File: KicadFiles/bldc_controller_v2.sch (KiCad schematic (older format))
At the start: 172 parts, among them J1 Conn_01x05_Male, J10 Conn_01x02_Female, J11 Conn_01x02_Female, J12 Conn_01x02_Female, J13 Conn_01x02_Female, J14 Conn_01x02_Female, J15 Conn_01x04_Male, J2 Conn_01x03_Male, J3 Conn_01x03_Male, J4 1935174, J5 Conn_01x02_Female, J9 Conn_01x02_Female, Q10 IRLB8721PBF, Q11 IRLB8721PBF, Q2 DMN65D8L-7, Q3 DMN65D8L-7, Q5 IRF4905, Q6 IRLB8721PBF, Q7 IRLB8721PBF, Q8 IRLB8721PBF, Q9 IRLB8721PBF, SW2 D6C40 F1 LFS, SW3 1301.9314, SW4 1301.9314, SW5 SW_Push_DPDT, U1 ATmega328P-PU, U2 uA7810, U3 LM7805_TO220, U4 MCP601-xP, U5 LM339, U6 IRS2004, U7 IRS2004, U8 IRS2004, U9 HCPL-181-00DE, Y1 9B-16.000MBBK-B

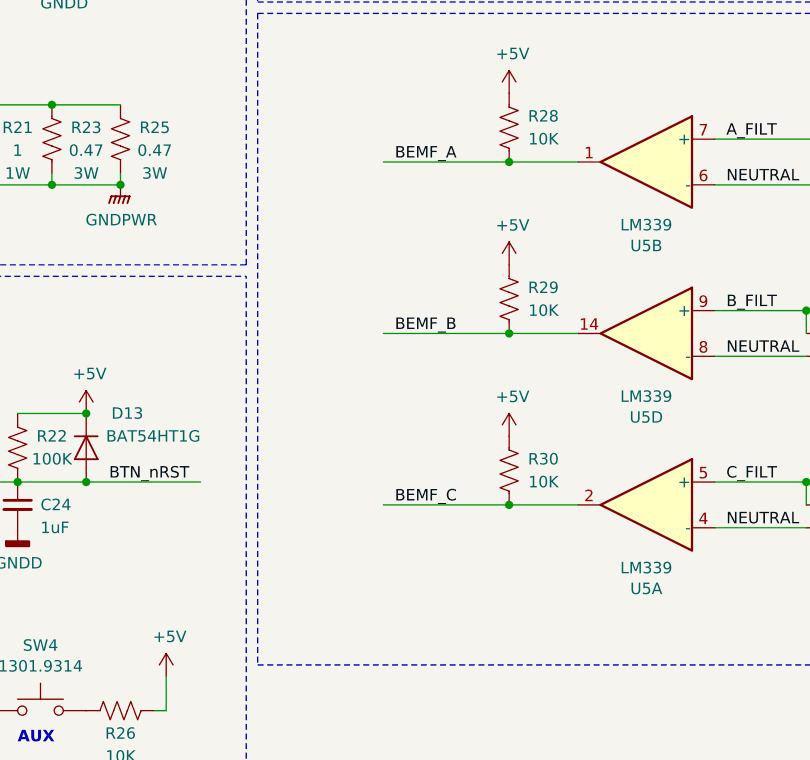
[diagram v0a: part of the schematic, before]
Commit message: Added Caps to BEMF Lines
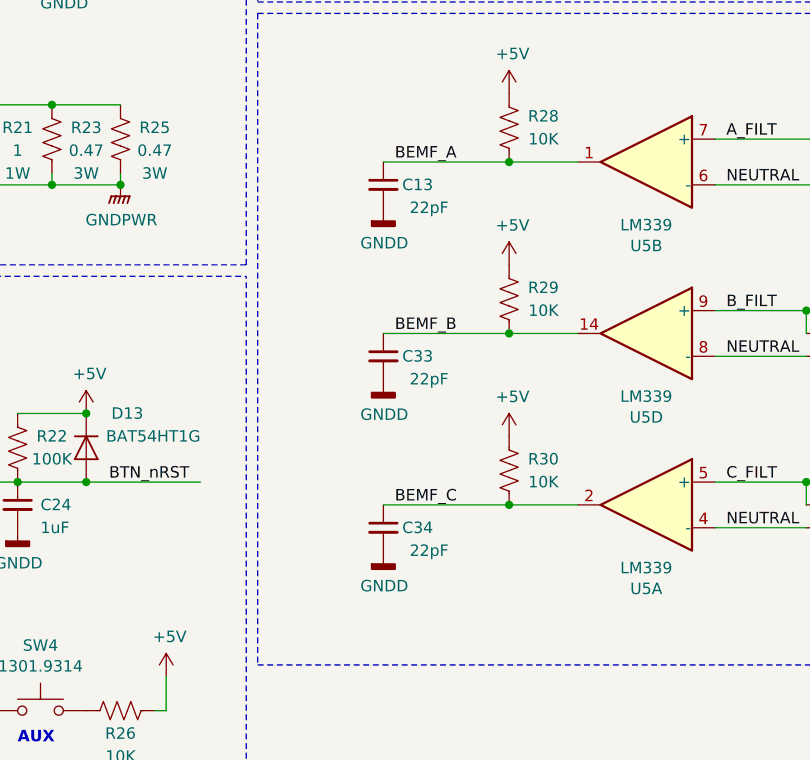
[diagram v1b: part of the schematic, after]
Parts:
- added C13, C33, C34: 22pF, Capacitor_SMD:C_0805_2012Metric_Pad1.15x1.40mm_HandSolder, symbol Device:C_Small
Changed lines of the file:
@@
 Wire Wire Line
 	8400 5850 8850 5850
+$Comp
+L Device:C_Small C33
+U 1 1 5E113FE6
+P 10500 7850
+F 0 "C33" H 10650 7850 50  0000 C CNN
+F 1 "22pF" H 10700 7750 50  0000 C CNN
+F 2 "Capacitor_SMD:C_0805_2012Metric_Pad1.15x1.40mm_HandSolder" H 10500 7850 50  0001 C CNN
+F 3 "~" H 10500 7850 50  0001 C CNN
+	1    10500 7850
+	1    0    0    -1
+$EndComp
+$Comp
+L power:GNDD #PWR026
+U 1 1 5E118132
+P 10500 7950
+F 0 "#PWR026" H 10500 7700 50  0001 C CNN
+F 1 "GNDD" H 10504 7795 50  0000 C CNN
+F 2 "" H 10500 7950 50  0001 C CNN
+F 3 "" H 10500 7950 50  0001 C CNN
+	1    10500 7950
+	1    0    0    -1
+$EndComp
+$Comp
+L Device:C_Small C34
+U 1 1 5E11899C
+P 10500 8600
+F 0 "C34" H 10650 8600 50  0000 C CNN
+F 1 "22pF" H 10700 8500 50  0000 C CNN
+F 2 "Capacitor_SMD:C_0805_2012Metric_Pad1.15x1.40mm_HandSolder" H 10500 8600 50  0001 C CNN
+F 3 "~" H 10500 8600 50  0001 C CNN
+	1    10500 8600
+	1    0    0    -1
+$EndComp
+$Comp
+L power:GNDD #PWR054
+U 1 1 5E1189A6
+P 10500 8700
+F 0 "#PWR054" H 10500 8450 50  0001 C CNN
+F 1 "GNDD" H 10504 8545 50  0000 C CNN
+F 2 "" H 10500 8700 50  0001 C CNN
+F 3 "" H 10500 8700 50  0001 C CNN
+	1    10500 8700
+	1    0    0    -1
+$EndComp
+$Comp
+L Device:C_Small C13
+U 1 1 5E13EF98
+P 10500 7100
+F 0 "C13" H 10650 7100 50  0000 C CNN
+F 1 "22pF" H 10700 7000 50  0000 C CNN
+F 2 "Capacitor_SMD:C_0805_2012Metric_Pad1.15x1.40mm_HandSolder" H 10500 7100 50  0001 C CNN
+F 3 "~" H 10500 7100 50  0001 C CNN
+	1    10500 7100
+	1    0    0    -1
+$EndComp
+$Comp
+L power:GNDD #PWR025
+U 1 1 5E13EFA2
+P 10500 7200
+F 0 "#PWR025" H 10500 6950 50  0001 C CNN
+F 1 "GNDD" H 10504 7045 50  0000 C CNN
+F 2 "" H 10500 7200 50  0001 C CNN
+F 3 "" H 10500 7200 50  0001 C CNN
+	1    10500 7200
+	1    0    0    -1
+$EndComp
 $EndSCHEMATC

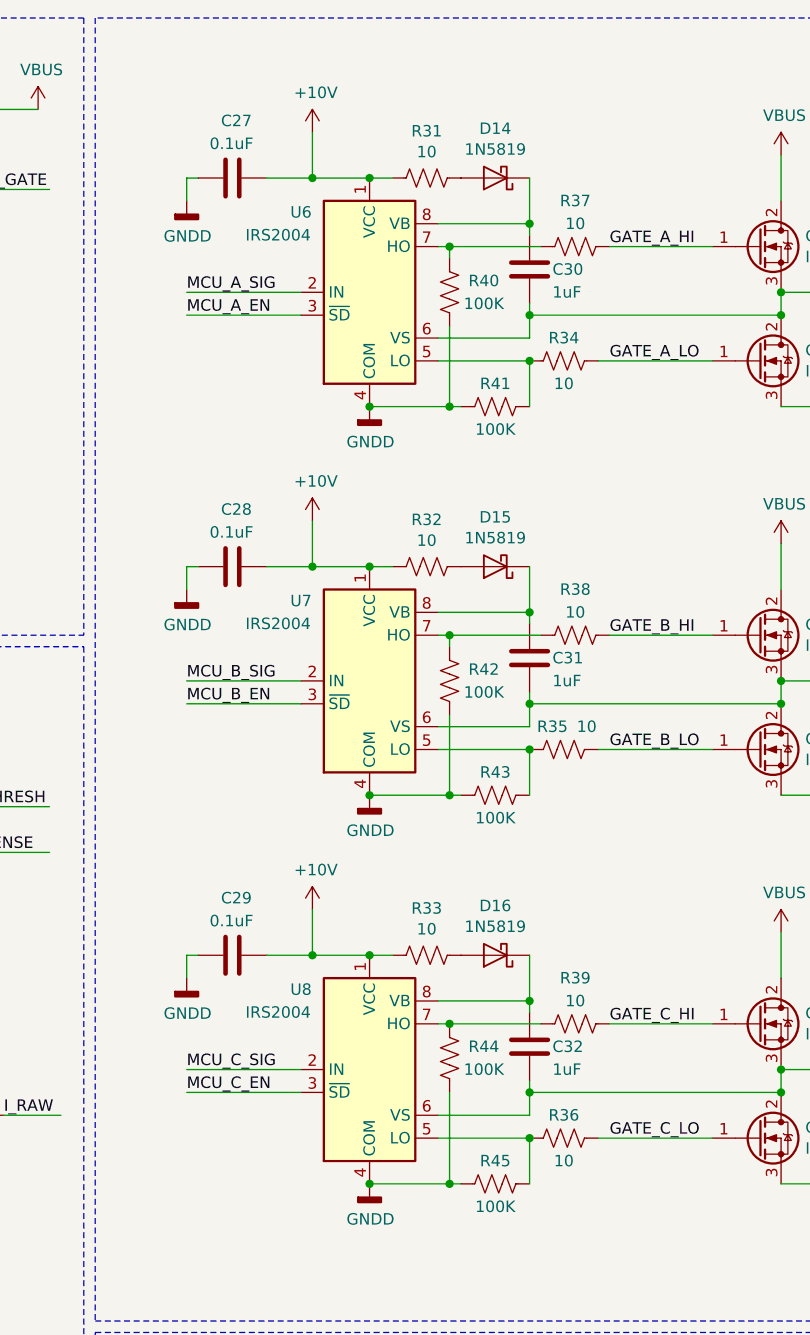
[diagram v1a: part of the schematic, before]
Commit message: Fixed Charge Pumps and Added Text
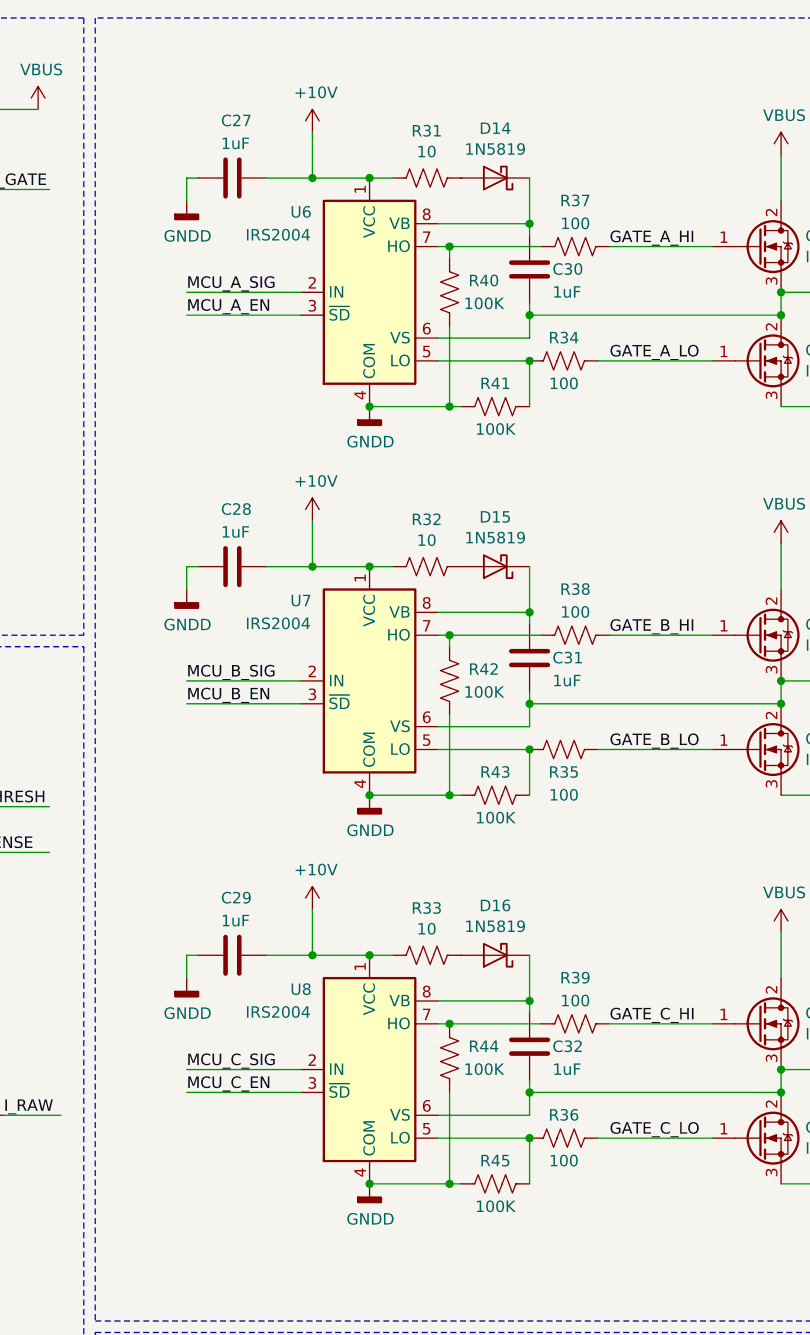
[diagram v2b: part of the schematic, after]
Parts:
- C27, C28, C29: value 0.1uF -> 1uF
- R34, R35, R36, R37, R38, R39: value 10 -> 100
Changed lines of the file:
@@
 P 10550 1300
 F 0 "C27" V 10300 1350 50  0000 R CNN
-F 1 "0.1uF" V 10400 1400 50  0000 R CNN
+F 1 "1uF" V 10400 1350 50  0000 R CNN
 F 2 "Capacitor_SMD:C_0805_2012Metric_Pad1.15x1.40mm_HandSolder" H 10588 1150 50  0001 C CNN
 F 3 "~" H 10550 1300 50  0001 C CNN
@@
 P 12050 1600
 F 0 "R37" V 11850 1600 50  0000 C CNN
-F 1 "10" V 11950 1600 50  0000 C CNN
+F 1 "100" V 11950 1600 50  0000 C CNN
 F 2 "Resistor_SMD:R_0805_2012Metric_Pad1.15x1.40mm_HandSolder" V 12090 1590 50  0001 C CNN
 F 3 "~" H 12050 1600 50  0001 C CNN
@@
 P 12000 2100
 F 0 "R34" V 11900 2100 50  0000 C CNN
-F 1 "10" V 12100 2100 50  0000 C CNN
+F 1 "100" V 12100 2100 50  0000 C CNN
 F 2 "Resistor_SMD:R_0805_2012Metric_Pad1.15x1.40mm_HandSolder" V 12040 2090 50  0001 C CNN
 F 3 "~" H 12000 2100 50  0001 C CNN
@@
 P 10550 3000
 F 0 "C28" V 10300 3050 50  0000 R CNN
-F 1 "0.1uF" V 10400 3100 50  0000 R CNN
+F 1 "1uF" V 10400 3050 50  0000 R CNN
 F 2 "Capacitor_SMD:C_0805_2012Metric_Pad1.15x1.40mm_HandSolder" H 10588 2850 50  0001 C CNN
 F 3 "~" H 10550 3000 50  0001 C CNN
@@
 P 12050 3300
 F 0 "R38" V 11850 3300 50  0000 C CNN
-F 1 "10" V 11950 3300 50  0000 C CNN
+F 1 "100" V 11950 3300 50  0000 C CNN
 F 2 "Resistor_SMD:R_0805_2012Metric_Pad1.15x1.40mm_HandSolder" V 12090 3290 50  0001 C CNN
 F 3 "~" H 12050 3300 50  0001 C CNN
@@
 U 1 1 6071FE0F
 P 12000 3800
-F 0 "R35" V 11900 3750 50  0000 C CNN
-F 1 "10" V 11900 3900 50  0000 C CNN
+F 0 "R35" V 12100 3800 50  0000 C CNN
+F 1 "100" V 12200 3800 50  0000 C CNN
 F 2 "Resistor_SMD:R_0805_2012Metric_Pad1.15x1.40mm_HandSolder" V 12040 3790 50  0001 C CNN
 F 3 "~" H 12000 3800 50  0001 C CNN
@@
 P 10550 4700
 F 0 "C29" V 10300 4750 50  0000 R CNN
-F 1 "0.1uF" V 10400 4800 50  0000 R CNN
+F 1 "1uF" V 10400 4750 50  0000 R CNN
 F 2 "Capacitor_SMD:C_0805_2012Metric_Pad1.15x1.40mm_HandSolder" H 10588 4550 50  0001 C CNN
 F 3 "~" H 10550 4700 50  0001 C CNN
@@
 P 12050 5000
 F 0 "R39" V 11850 5000 50  0000 C CNN
-F 1 "10" V 11950 5000 50  0000 C CNN
+F 1 "100" V 11950 5000 50  0000 C CNN
 F 2 "Resistor_SMD:R_0805_2012Metric_Pad1.15x1.40mm_HandSolder" V 12090 4990 50  0001 C CNN
 F 3 "~" H 12050 5000 50  0001 C CNN
@@
 P 12000 5500
 F 0 "R36" V 11900 5500 50  0000 C CNN
-F 1 "10" V 12100 5500 50  0000 C CNN
+F 1 "100" V 12100 5500 50  0000 C CNN
 F 2 "Resistor_SMD:R_0805_2012Metric_Pad1.15x1.40mm_HandSolder" V 12040 5490 50  0001 C CNN
 F 3 "~" H 12000 5500 50  0001 C CNN
